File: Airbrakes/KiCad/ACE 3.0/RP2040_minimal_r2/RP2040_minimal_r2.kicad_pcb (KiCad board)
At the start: 2 copper layers, 52 x 51 mm, 45 parts, among them J1 USB_B_Micro, J2 Conn_01x02, J3 104031-0811, J4 Conn_02x18_Odd_Even, U1 NCP1117-3.3_SOT223, U2 W25Q128JVS, U3 RP2040, U4 BMI088, U5 BMP581, U6 BMM350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

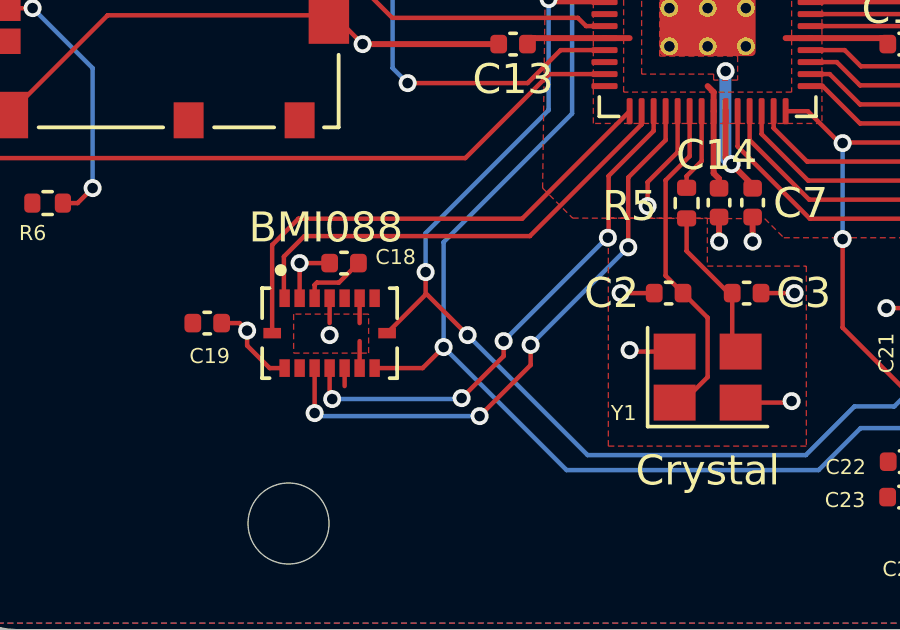
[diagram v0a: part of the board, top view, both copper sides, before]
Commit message: minor via location change
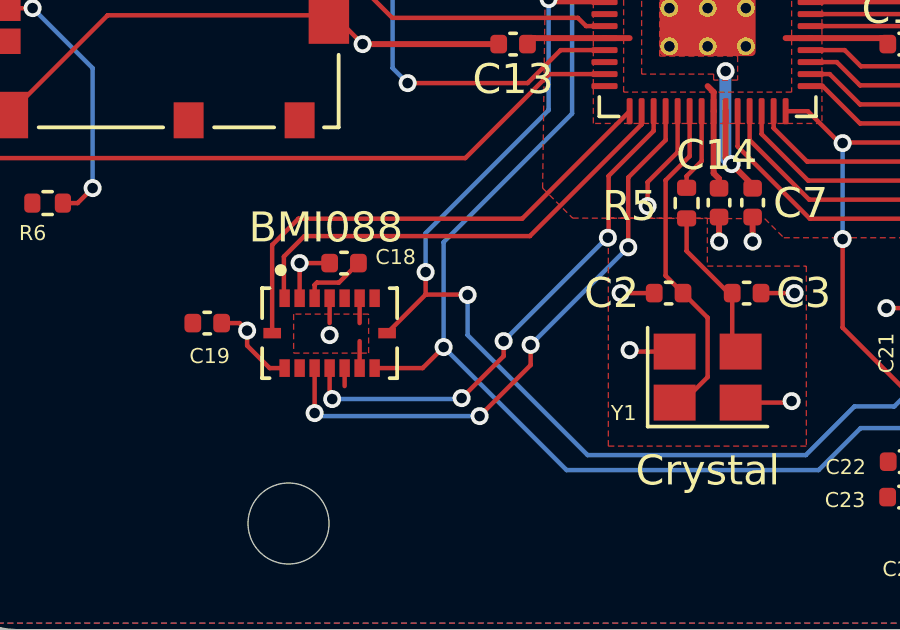
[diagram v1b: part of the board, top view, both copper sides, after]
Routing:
- net /SCL: track 42.5 -> 43.3 mm
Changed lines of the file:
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@@
+	)
+	(segment
+		(start 92 109.56)
+		(end 91.99 109.55)
+		(width 0.15)
+		(layer "F.Cu")
+		(net 44)
 	)
 	(segment
@@
 	)
 	(segment
-		(start 96.5625 99.8)
-		(end 94.8 99.8)
+		(start 91.99 109.55)
+		(end 90.6 109.55)
 		(width 0.15)
 		(layer "F.Cu")
@@
 	)
 	(segment
-		(start 90.6 109.55)
-		(end 90.65 109.55)
+		(start 96.5625 99.8)
+		(end 94.8 99.8)
 		(width 0.15)
 		(layer "F.Cu")
@@
 		(start 110.2 114.9999)
 		(end 110 115.1999)
-		(width 0.15)
-		(layer "F.Cu")
-		(net 44)
-	)
-	(segment
-		(start 90.65 109.55)
-		(end 92 110.9)
 		(width 0.15)
 		(layer "F.Cu")
@@
 	)
 	(via
-		(at 92 110.9)
+		(at 92 109.56)
 		(size 0.6)
 		(drill 0.35)
@@
 		(start 104.893958 113.278854)
 		(end 106.221146 113.278854)
-		(width 0.15)
-		(layer "B.Cu")
-		(net 44)
-	)
-	(segment
-		(start 106.221146 113.278854)
-		(end 107.6 111.9)
 		(width 0.15)
 		(layer "B.Cu")
@@
 		(start 108.5 113.5)
 		(end 108.9 113.9)
+		(width 0.15)
+		(layer "B.Cu")
+		(net 44)
+	)
+	(segment
+		(start 92 109.56)
+		(end 92 110.9)
+		(width 0.15)
+		(layer "B.Cu")
+		(net 44)
+	)
+	(segment
+		(start 106.221146 113.278854)
+		(end 107.6 111.9)
 		(width 0.15)
 		(layer "B.Cu")
@@
 	)
 	(segment
-		(start 92 110.9)
-		(end 96 114.9)
+		(start 103.272812 114.9)
+		(end 104.893958 113.278854)
 		(width 0.15)
 		(layer "B.Cu")
@@
 	)
 	(segment
-		(start 103.272812 114.9)
-		(end 104.893958 113.278854)
+		(start 92 110.9)
+		(end 96 114.9)
 		(width 0.15)
 		(layer "B.Cu")
